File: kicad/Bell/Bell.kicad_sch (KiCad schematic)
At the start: 10 parts, among them J1 Jack-DC, Q1 Q_NMOS_GDS, U1 NodeMCUv3

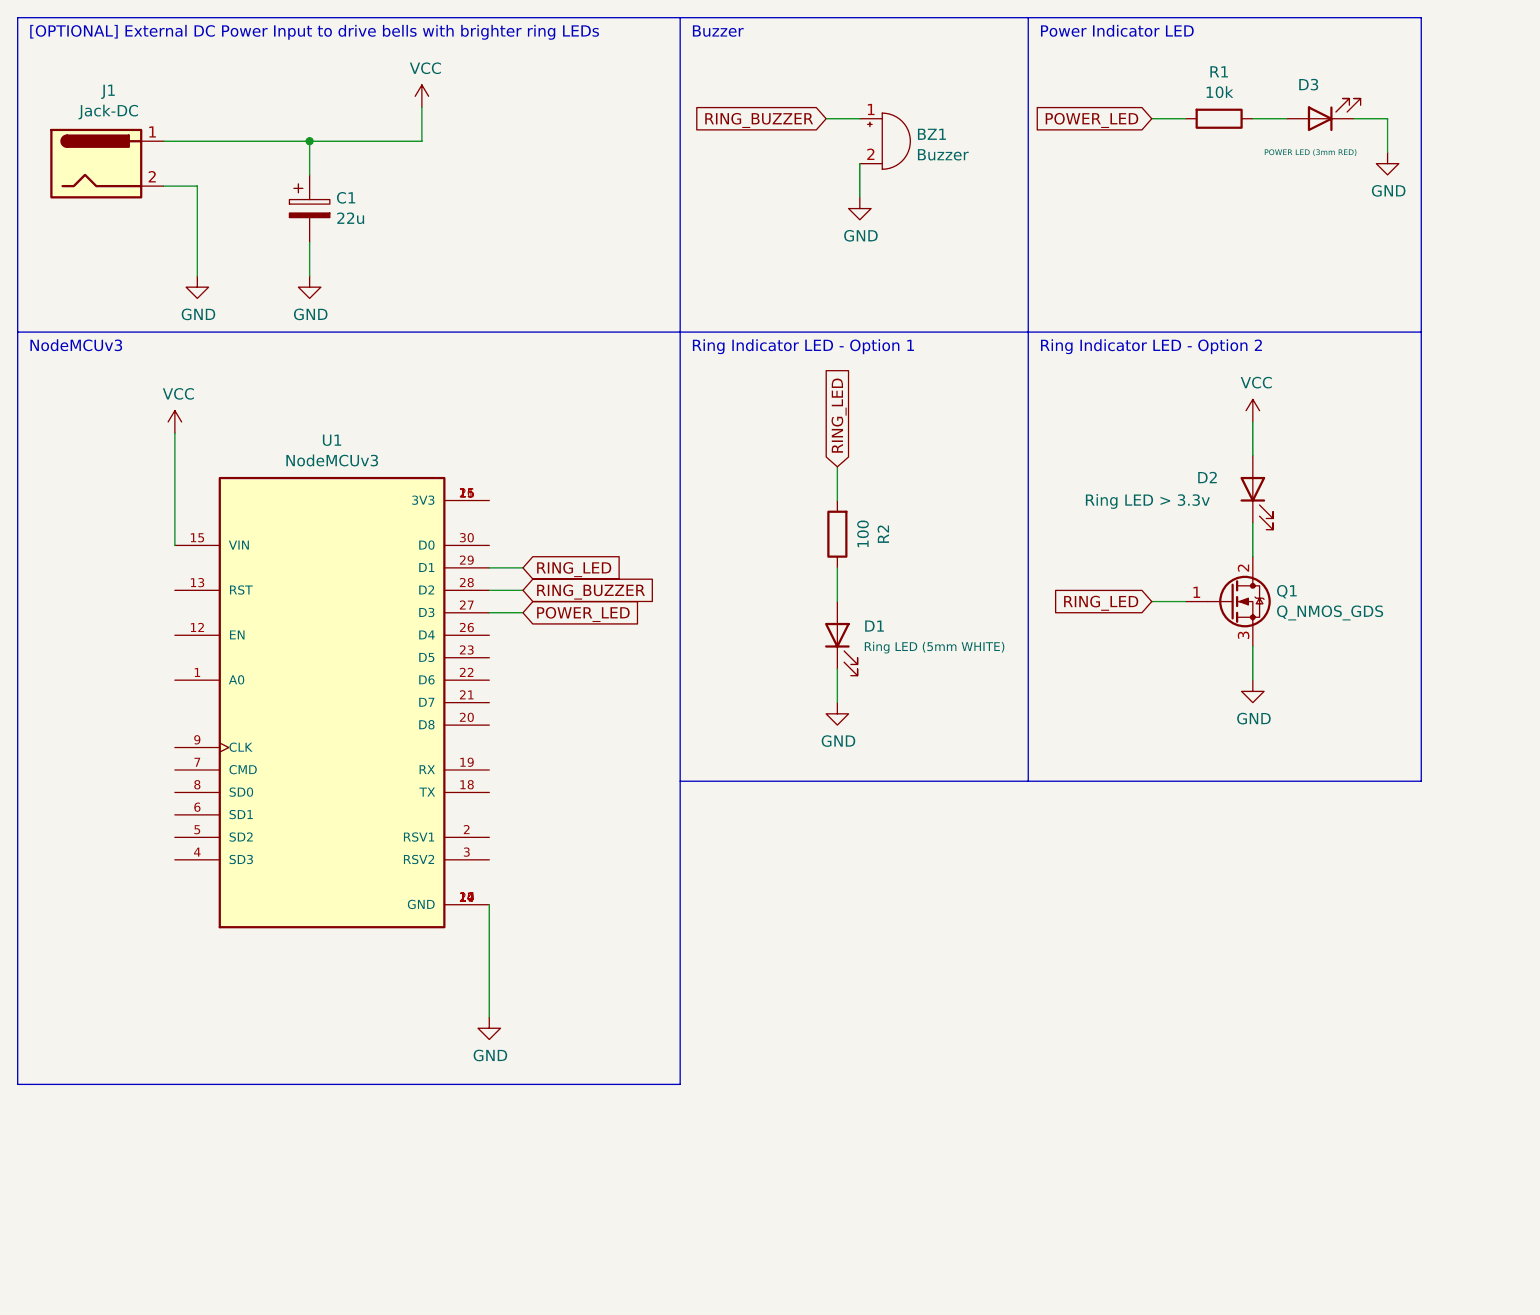
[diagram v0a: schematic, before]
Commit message: README: Added images
Signed-off-by: Patrick Pedersen <ctx.xda@gmail.com>
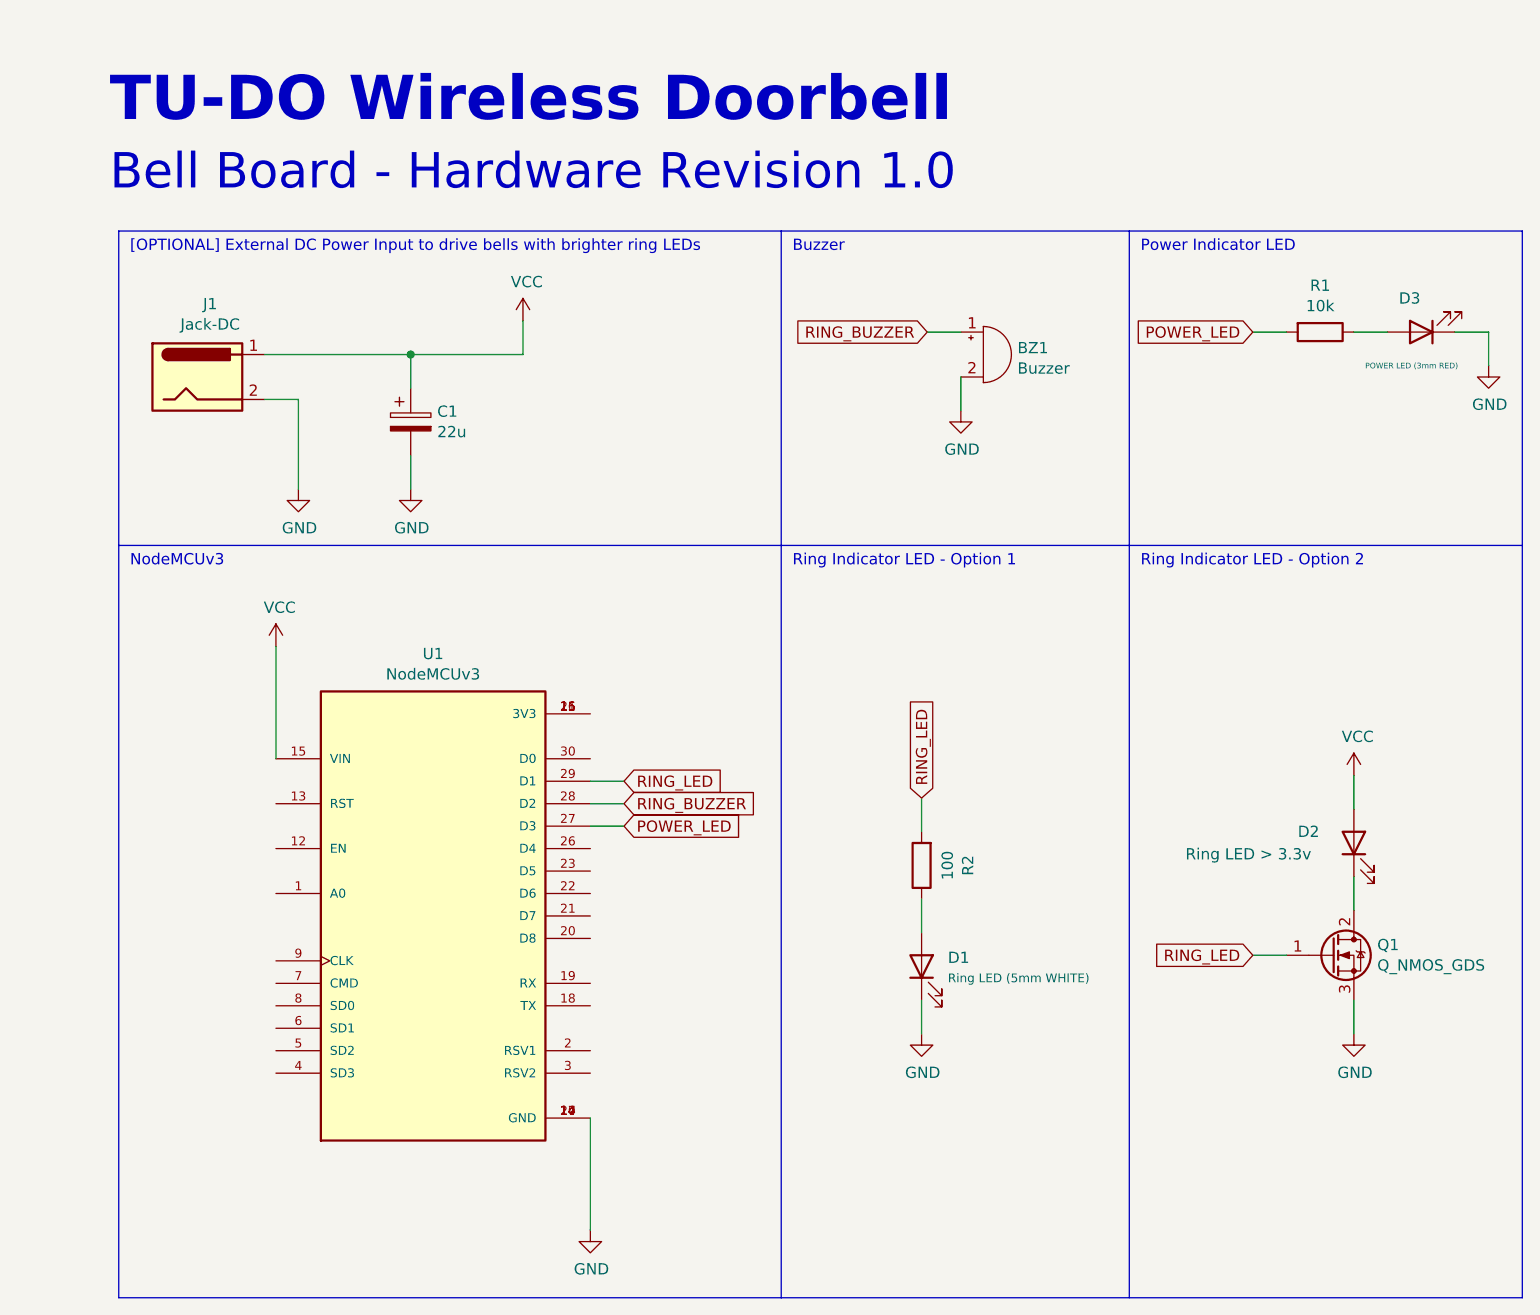
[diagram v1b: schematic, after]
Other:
- note added: "Bell Board - Hardware Revision 1.0"
- note added: "TU-DO Wireless Doorbell"
- moved on the sheet: BZ1, C1, D1, D2, D3, J1, Q1, R1, R2, U1
